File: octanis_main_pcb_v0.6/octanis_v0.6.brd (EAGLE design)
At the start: 80 x 48 mm, 103 parts, among them IC1 BME280, IC2 BNO055A, Q1 32.768kHz, Q2 32.768kHz, U1 TPS61232, U10 INA210, U11 INA210, U12 INA210, U13 RN2483, U2 DRV8836DSSR, U3 DRV8836DSSR, U4 MSP432, U5 SST25VF064C, U6 DRV8836DSSR, U7 DRV8836DSSR, U8 MAX6001SOT-23, U9 INA210

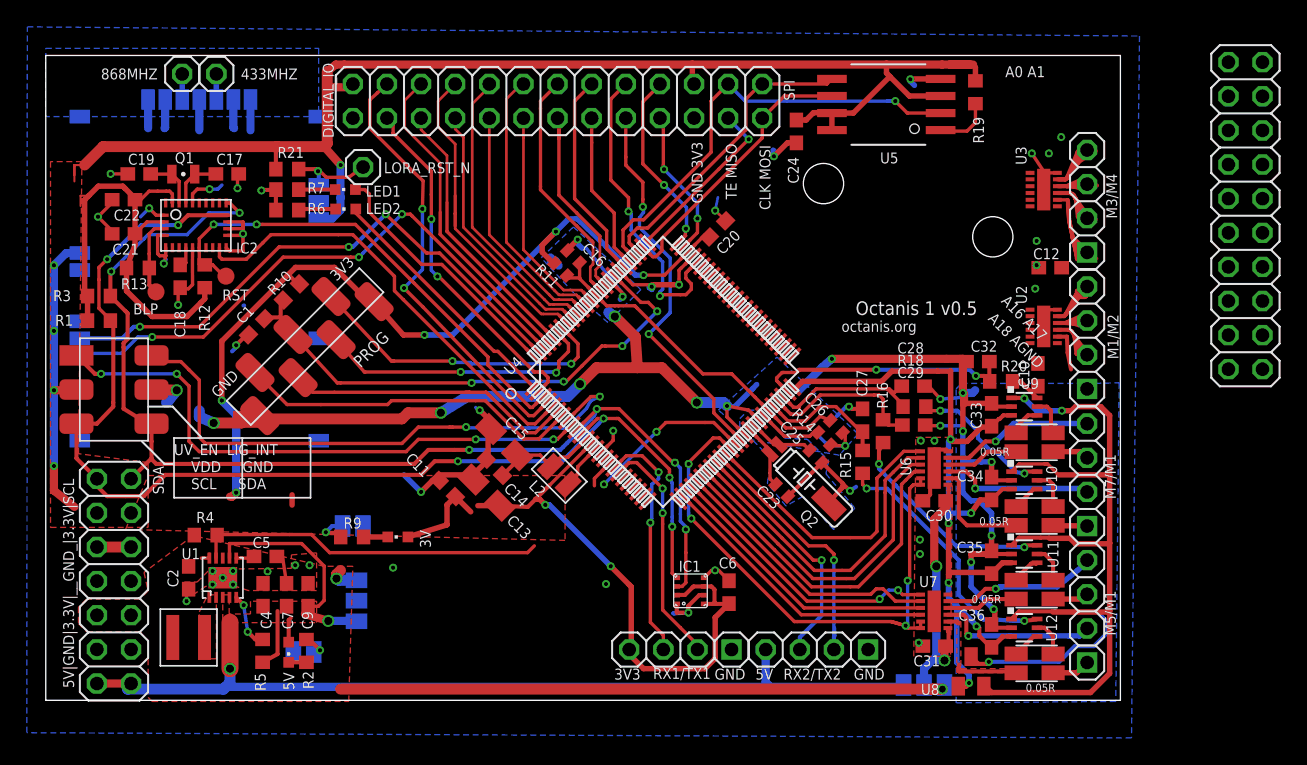
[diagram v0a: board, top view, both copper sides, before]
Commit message: finalized changes for v0.6. coax connector missing
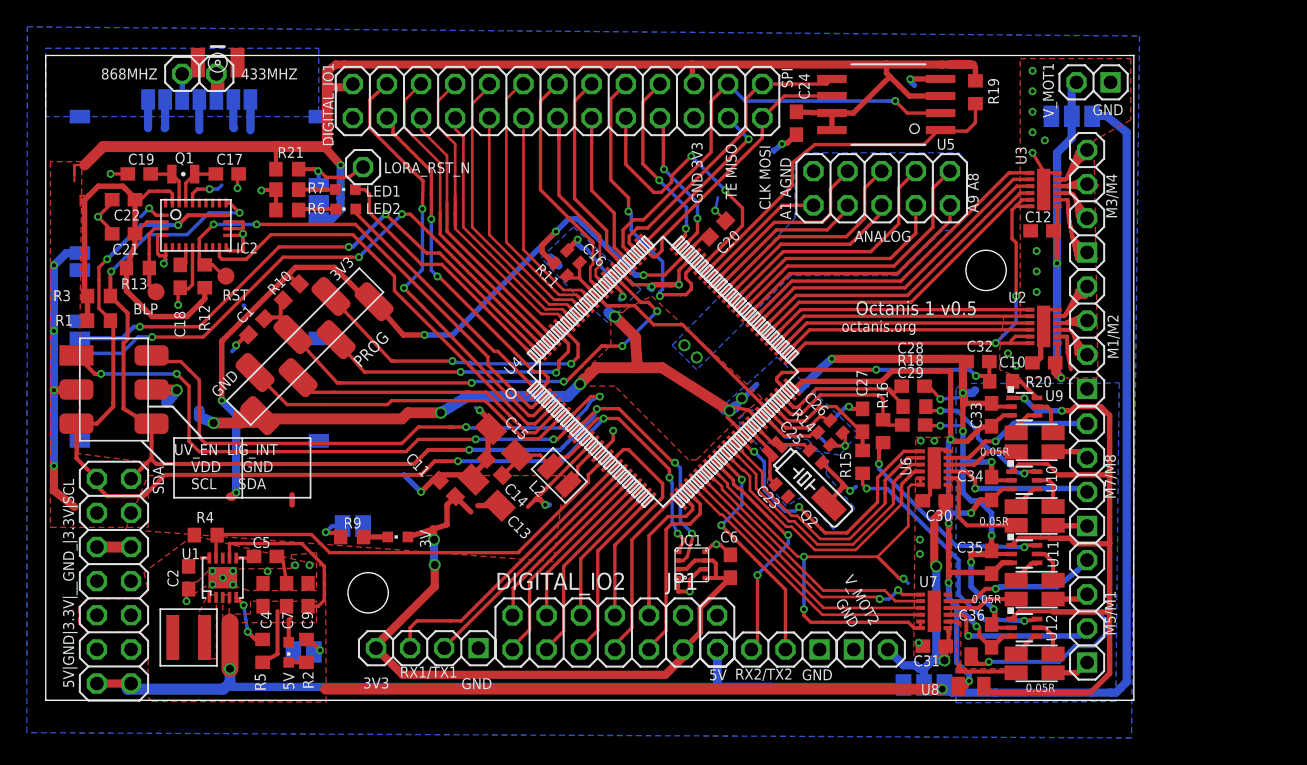
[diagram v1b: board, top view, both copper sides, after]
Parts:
- added DIGITAL_IO2: (no value), pinhead:2X05
- added JP1: (no value), pinhead:2X02
- added V_MOT1, V_MOT2: (no value), pinhead-2:1X02-S
- added X1: MC-921, con-coax:MC-921
- ANALOG: device pinhead:2X10 -> pinhead:2X05
- moved VMOT_SEL 64.3 mm to (76.4, 44.5), turned to 0 degrees
- moved ANALOG 27.2 mm to (62.2, 39.1), turned to 0 degrees
- moved RX1/TX1 18.8 mm to (28.4, 4.88)
- moved RX2/TX2 3.61 mm to (53.8, 4.78)
- moved C12 2.81 mm to (74.2, 35.9)
- moved C6 1.93 mm to (51.0, 11.0)
- moved IC1 1.93 mm to (48.1, 11.1)
- moved C10 0.99 mm to (74.3, 26.1), turned to 0 degrees
- moved C24 0.61 mm to (55.9, 44.0)
- renumbered DIGITAL_IO to DIGITAL_IO1, M7/M1 to M7/M8
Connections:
- removed net A0: ANALOG.1
- removed net P3.7: DIGITAL_IO1.6, U4.39
- removed net P5.6_NC: U4.70
- new net P10.4: DIGITAL_IO2.6, U4.24
- new net P10.5: DIGITAL_IO2.5, U4.25
- new net P2.1: DIGITAL_IO2.8, U4.17
- new net P2.4: DIGITAL_IO2.2, U4.20
- new net P2.5: DIGITAL_IO2.1, U4.21
- new net P2.6: DIGITAL_IO2.4, U4.22
- new net P2.7: DIGITAL_IO2.3, U4.23
- new net P5.6: DIGITAL_IO1.6, U4.70
- new net P7.4: DIGITAL_IO2.7, U4.26
- new net P7.5: DIGITAL_IO2.10, U4.27
- new net P7.6: DIGITAL_IO2.9, U4.28
- net +3V3: now also JP1.1
- net +5V: now also JP1.3; no longer VMOT_SEL.3
- net 5VEN: now also U4.16; no longer U4.17
- net A1: now also ANALOG.1; no longer ANALOG.2
- net A2: now also ANALOG.4; no longer ANALOG.3
- net A3: now also ANALOG.3; no longer ANALOG.4
- net A4: now also ANALOG.6; no longer ANALOG.5
- net A5: now also ANALOG.5; no longer ANALOG.6
- net A6: now also ANALOG.8; no longer ANALOG.7
- net A7: now also ANALOG.7; no longer ANALOG.8
- net A8: now also ANALOG.10; no longer ANALOG.9
- net A9: now also ANALOG.9; no longer ANALOG.10
- net AGND: now also ANALOG.2
- net GND: now also JP1.2, JP1.4, V_MOT1.1, V_MOT2.1, X1.2@1, X1.2@2
- net M1234SLEEP: no longer U4.16
- net M1IN1: no longer U4.38
- net M1IN2: no longer U4.20
- net M2IN1: no longer U4.21
- net M2IN2: no longer U4.22
- net M3IN1: no longer U4.23
- net M3IN2: no longer U4.24
- net M4IN1: no longer U4.25
- net M4IN2: no longer U4.26
- net M5678SLEEP: now also U4.33; no longer U4.37
- net M5IN1: now also U4.29; no longer U4.27
- net M5IN2: now also U4.30; no longer U4.28
- net M6IN1: now also U4.32; no longer U4.30
- net M6IN2: now also U4.31; no longer U4.29
- net M7IN1: now also U4.36; no longer U4.31
- net M7IN2: now also U4.37; no longer U4.32
- net M8IN1: now also U4.38; no longer U4.33
- net M8IN2: now also U4.39; no longer U4.36
- net V_MOTOR: now also V_MOT1.2
- net V_MOTOR2: now also V_MOT2.2
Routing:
- net 3V3_MODULE2: track 49.1 -> 106.0 mm, vias 2 -> 1
- net M1234SLEEP: track 0.00 -> 33.8 mm, vias 0 -> 2
- net V_MOTOR: track 0.00 -> 30.1 mm, vias 0 -> 2
- net P3.7: track 29.4 -> 0.00 mm, vias 2 -> 0
- net M4IN2: track 0.03 -> 25.0 mm
- net M4IN1: track 0.00 -> 24.6 mm
- net M3IN2: track 0.00 -> 24.2 mm
- net M3IN1: track 0.00 -> 23.8 mm
- net SPI_FLASH_CS: track 4.30 -> 26.9 mm
- net P5.6: track 0.00 -> 21.6 mm, vias 0 -> 2
- net A8: track 0.00 -> 21.2 mm
- net M2IN2: track 0.00 -> 20.0 mm
- net M2IN1: track 0.00 -> 19.6 mm
- net M1IN2: track 0.00 -> 19.1 mm
- net A9: track 0.00 -> 18.9 mm
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- added copper zone on layer 1, net AGND
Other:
- board size 80 x 48 mm -> 81 x 48 mm
- board text added: "A1 AGND"
- board text added: "A9 A8"
- board text removed: "A0 A1"
- board text removed: "A16 A17"
- board text removed: "A18 AGND"

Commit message: added SMA connector for LoRa
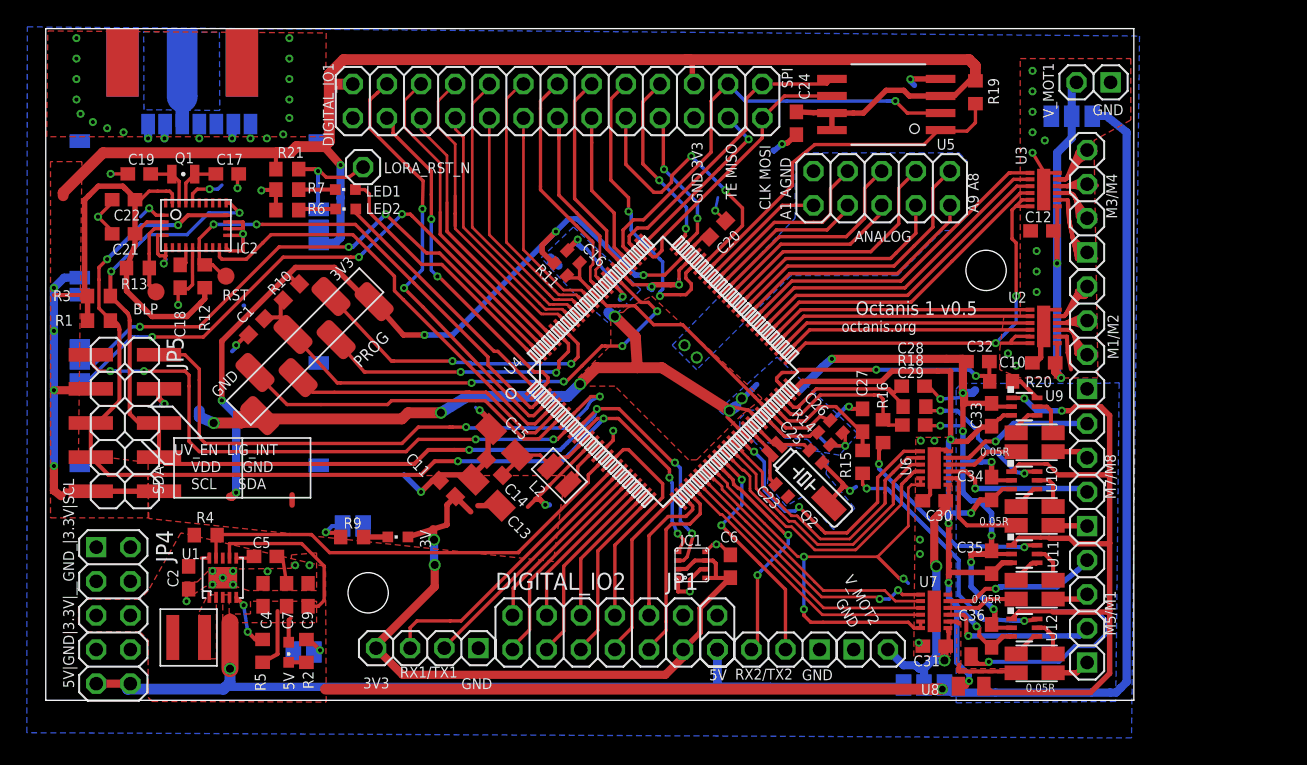
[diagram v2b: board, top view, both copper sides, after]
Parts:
- removed 433MHZ, 868MHZ: (no value), Headerlibrary:1X01
- removed J1: (no value), Seeed-OPL-Connector:H2X3-SMD-2.54
- removed JP2: (no value), pinhead:2X07
- removed X1: MC-921, con-coax:MC-921
- added JP4: (no value), pinhead-2:2X05
- added JP5: (no value), pinhead-2:2X05SMD
- added X3: (no value), sma_end_launch:SMA_EDGELAUNCH
- moved U13 1.83 mm to (20.3, 17.2)
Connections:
- net +3V3: now also JP5.10, JP5.3, JP5.9; no longer J1.2, JP2.3, JP2.4
- net +5V: now also JP4.10, JP4.9; no longer JP2.13, JP2.14
- net 3V3_MODULE2: now also JP4.5, JP4.6; no longer JP2.10, JP2.9
- net ANT433: no longer 433MHZ.1
- net ANT868: now also X3.P; no longer 868MHZ.1
- net EXT_LIGHTNING_INT: now also JP5.2; no longer J1.6
- net EXT_UV_EN: now also JP5.1; no longer J1.1
- net GND: now also JP4.1, JP4.2, JP4.3, JP4.4, JP4.7, JP4.8, JP5.4, X3.GND@1, X3.GND@2, X3.GND@3, X3.GND@4; no longer J1.5, JP2.11, JP2.12, JP2.5, JP2.6, JP2.7, JP2.8, X1.2@1, X1.2@2
- net SCL: now also JP5.5, JP5.7; no longer J1.3, JP2.1
- net SDA: now also JP5.6, JP5.8; no longer J1.4, JP2.2
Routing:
- net GND: track 122.4 -> 111.5 mm, vias 43 -> 63
- net +3V3: track 298.7 -> 305.1 mm
- net ANT868: track 1.91 -> 6.42 mm
- net SCL: track 86.6 -> 84.2 mm
- net ANT433: track 1.91 -> 0.00 mm
- net LORA_RST_N: track 6.32 -> 8.22 mm
- net SDA: track 84.5 -> 82.9 mm
- net RX3: track 42.9 -> 43.7 mm
- net TX3: track 42.2 -> 42.9 mm
- net +5V: track 95.0 -> 94.3 mm
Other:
- board size 81 x 48 mm -> 81 x 50 mm

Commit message: DRC clean layout
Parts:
- moved U$1 1.75 mm to (16.4, 18.1)
- moved V_MOT1 1.30 mm to (76.8, 47.5)
- moved R4 0.54 mm to (11.5, 12.9)
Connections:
- new net V_MOTOR_ALT: VMOT_SEL.3, V_MOT1.2
- net V_MOTOR: no longer V_MOT1.2
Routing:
- net GND: track 111.5 -> 115.2 mm
- net V_MOTOR_ALT: track 0.00 -> 3.25 mm
- net M5678SLEEP: track 40.0 -> 36.9 mm, vias 3 -> 2
- net V_MOTOR: track 30.1 -> 27.4 mm
- net N$49: track 3.18 -> 5.02 mm
- net N$39: track 3.10 -> 4.55 mm
- net M7IN2: track 21.1 -> 22.1 mm
- net 5VEN: track 34.5 -> 35.5 mm
- net M8IN2: track 21.4 -> 22.3 mm
- net M8IN1: track 21.0 -> 21.8 mm
- net M7IN1: track 21.7 -> 22.5 mm
- net 3V3_MODULE2: track 106.0 -> 105.4 mm
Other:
- board text added: "5V|GND|3.3V|__GND_|"
- board text added: "A8 A9"
- board text added: "AGND A1"
- board text added: "Octanis 1 v0.6"
- board text removed: "5V|GND|3.3V|__GND_|3.3V|SCL"
- board text removed: "A1 AGND"
- board text removed: "A9 A8"
- board text removed: "Octanis 1 v0.5"
- board text removed: "SDA"

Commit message: revised silklayer
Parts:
- removed C35, C36: 10n, rcl:C0603
- removed JP4: (no value), pinhead-2:2X05
- removed R20: 6.8k, rcl:R0603
- removed R21: 100k, rcl:R0603
- added C3: 100n, rcl:C0603
- added C8: 22uF, rcl:C0603
- added JP3: (no value), pinhead:2X02
- added R17: 6.8k, rcl:R0603
- added R8: 1k, rcl:R0603
- C1: value 1n -> 22uF
- C10: value 470n -> 10nF
- C11: value 100n -> 1n
- C12: value 470n -> 10u; device rcl:C0603 -> rcl:A/3216-18R
- C13: value 10u -> 100n; device rcl:A/3216-18R -> rcl:C0603
- C17: value 12p -> 100n
- C18: value 100n -> 12p; device rcl:C0603 -> rcl:C0402
- C19, C20: device rcl:C0603 -> rcl:C0402
- C2: value 22uF -> 100n
- C22: value 120n -> 100n
- C23: value 12p -> 470n; device rcl:C0402 -> rcl:C0603
- C24: value 100n -> 10n
- C25: value 12p -> 10n; device rcl:C0402 -> rcl:C0603
- C26: value 100n -> 470n; device rcl:C0402 -> rcl:C0603
- C27, C30: value 470n -> 10n
- C33, C34: value 10n -> 470n
- C4: value 22uF -> 120n
- C5: value 10nF -> 12p
- C6: value 100n -> 12p
- IC1: value BME280 -> BNO055A; device bosch-bme280:BME280 -> BNO055:BNO055
- IC2: value BNO055A -> BME280; device BNO055:BNO055 -> bosch-bme280:BME280
- JP1: device pinhead:2X02 -> pinhead-2:2X05
- LED1: value LED0 -> LED1
- LED2: value LED1 -> LED0
- R1: value 4.7k -> 1M
- R10: value 47k -> 1k
- R11: value 0R -> 1k; device rcl:R0402 -> rcl:R0603
- R13: value 100k -> 0R; device rcl:R0603 -> rcl:R0402
- R18: value 6.8k -> 10k
- R19: value 10k -> 6.8k
- R2: value 1k -> 4.7k
- R4, R5: value 1M -> 100k
- R7: value 1k -> 1M
- R9: value 1k -> 47k
- U11, U12: value INA210 -> DRV8836DSSR; device Octanis1_EPS:SC70-6 -> DRV8834:SON50P200X300X80-13N
- U2: value DRV8836DSSR -> MSP432; device DRV8834:SON50P200X300X80-13N -> MSP-EXP432:PZ100
- U3: value DRV8836DSSR -> MAX6001SOT-23; device DRV8834:SON50P200X300X80-13N -> Octanis1:MAX6001
- U4: value MSP432 -> DRV8836DSSR; device MSP-EXP432:PZ100 -> DRV8834:SON50P200X300X80-13N
- U5: value SST25VF064C -> DRV8836DSSR; device BertaLib:SOIC_8-LEAD -> DRV8834:SON50P200X300X80-13N
- U6: value DRV8836DSSR -> SST25VF064C; device DRV8834:SON50P200X300X80-13N -> BertaLib:SOIC_8-LEAD
- U7: value DRV8836DSSR -> INA210; device DRV8834:SON50P200X300X80-13N -> Octanis1_EPS:SC70-6
- U8: value MAX6001SOT-23 -> INA210; device Octanis1:MAX6001 -> Octanis1_EPS:SC70-6
- moved C10 59.7 mm to (16.4, 11.7)
- moved C19 54.6 mm to (57.3, 19.2), turned to 135 degrees
- moved C22 50.4 mm to (55.9, 44.0), turned to 270 degrees
- moved C18 47.5 mm to (54.8, 16.6), turned to 135 degrees
- moved C17 47.5 mm to (51.0, 11.0), turned to 90 degrees
- moved C6 47.5 mm to (13.5, 40.2), turned to 0 degrees
- moved C12 45.7 mm to (32.8, 16.5), turned to 315 degrees
- moved V_MOT1 45.4 mm to (61.4, 4.78), turned to 0 degrees
- moved V_MOT2 45.4 mm to (76.8, 47.5), turned to 180 degrees
- moved IC1 44.7 mm to (11.2, 36.4), turned to 90 degrees
- moved IC2 44.7 mm to (48.1, 11.1), turned to 270 degrees
- moved C21 44.2 mm to (50.0, 36.1), turned to 225 degrees
- moved JP1 43.7 mm to (5.03, 7.32), turned to 270 degrees
- moved C24 40.8 mm to (70.4, 5.79)
- moved U3 36.3 mm to (68.9, 3.15), turned to 0 degrees
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- renumbered JP5 to JP2, M5/M1 to M5/M6, U$100 to U$2, U13 to U100, VMOT_SEL2 to VMOT_SEL100, X3 to 868MHZ
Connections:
- net +3V3: now also C12.+, C13.2, C17.1, C21.2, C3.1, C4.1, IC1.28, IC1.3, IC2.2, IC2.6, IC2.8, JP3.1, R12.2, R18.2, R2.2, R4.1, R5.2, R9.1, U2.13, U2.73, U6.RST/HOLD, U6.VDD, U6.WP; no longer C11.2, C13.+, C20.2, C21.1, C24.1, C6.1, IC1.2, IC1.6, IC1.8, IC2.28, IC2.3, JP1.1, R1.2, R10.1, R11.2, R12.1, R19.2, R21.2, U4.13, U4.73, U5.RST/HOLD, U5.VDD, U5.WP
- net +5V: now also C8.1, JP1.10, JP1.9, JP3.3, R7.2; no longer C4.1, JP1.3, JP4.10, JP4.9, R5.2
- net 3V3_MODULE2: now also C1.1, JP1.5, JP1.6, R1.2; no longer C2.1, JP4.5, JP4.6, R4.2
- net 5VEN: now also R1.1, U2.16; no longer R4.1, U4.16
- net A1: now also U2.68; no longer U4.68
- net A2: now also U2.67; no longer U4.67
- net A20: now also R19.1, U2.49; no longer R20.1, U4.49
- net A20UNF: now also R19.2, U10.6; no longer R20.2, U9.6
- net A21: now also C31.2, R17.1, U2.48; no longer C28.2, R18.1, U4.48
- net A21UNF: now also R17.2, U9.6; no longer R18.2, U10.6
- net A22: now also C28.2, U2.47; no longer C29.2, U4.47
- net A22UNF: now also U8.6; no longer U11.6
- net A23: now also C29.2, U2.46; no longer C27.2, U4.46
- net A23UNF: now also U7.6; no longer U12.6
- net A3: now also U2.66; no longer U4.66
- net A4: now also U2.65; no longer U4.65
- net A5: now also U2.64; no longer U4.64
- net A6: now also U2.63; no longer U4.63
- net A7: now also U2.62; no longer U4.62
- net A8: now also U2.61; no longer U4.61
- net A9: now also U2.60; no longer U4.60
- net ACCEL_INT: now also IC1.14, U2.5; no longer IC2.14, U4.5
- net ACCEL_N_BOOTLD: now also IC1.4, R5.1; no longer IC2.4, R13.1
- net ACCEL_N_RST: now also IC1.11, R4.2, U2.3; no longer IC2.11, R12.2, U4.3
- net AGND: now also C20.2, C24.1, C25.1, C30.1, C31.1, U2.40, U2.43, U2.84, U3.3, U7.2, U8.2; no longer C26.2, C33.1, C34.1, C35.1, C36.1, U11.2, U12.2, U4.40, U4.43, U4.84, U8.3
- net AVCC: now also C20.1, R13.1, U2.45, U2.87; no longer C26.1, R11.1, U4.45, U4.87
- net CURR_SENSE_EN: now also C24.2, C25.2, C27.2, C30.2, U2.50, U3.1, U7.3, U8.3; no longer C33.2, C34.2, C35.2, C36.2, U11.3, U12.3, U4.50, U8.1
- net EXT_LIGHTNING_INT: now also U2.8; no longer U4.8
- net EXT_UV_EN: now also U2.9; no longer U4.9
- net GND: now also C1.2, C10.2, C12.-, C13.1, C19.1, C2.1, C21.1, C26.1, C3.2, C33.1, C34.1, C8.2, IC1.10, IC1.15, IC1.16, IC1.17, IC1.18, IC1.2, IC1.25, IC1.6, IC2.1, IC2.7, JP1.1, JP1.3, JP1.7, JP1.8, JP3.2, JP3.4, R10.1, R11.1, U11.13, U11.6, U12.13, U12.6, U2.15, U2.72, U2.82, U4.13, U4.6, U5.13, U5.6, U6.VSS; no longer C1.1, C10.1, C12.1, C13.-, C19.2, C2.2, C20.1, C21.2, C24.2, C25.1, C30.1, C31.1, IC1.1, IC1.7, IC2.10, IC2.15, IC2.16, IC2.17, IC2.18, IC2.2, IC2.25, IC2.6, JP4.1, JP4.2, JP4.3, JP4.4, JP4.7, JP4.8, R6.1, R7.1, U2.13, U2.6, U3.13, U3.6, U4.15, U4.72, U4.82, U5.VSS, U6.13, U6.6, U7.13, U7.6
- net LED0: now also LED2.A, U2.100; no longer LED1.A, U4.100
- net LED1: now also LED1.A, U2.1; no longer LED2.A, U4.1
- net LORA_RST_N: now also R12.1; no longer R21.1
- net M1234SLEEP: now also U11.11, U11.12, U12.11, U12.12, U2.51; no longer U2.11, U2.12, U3.11, U3.12, U4.51
- net M1IN1: now also U11.10, U2.52; no longer U2.10, U4.52
- net M1IN2: now also U11.9, U2.53; no longer U2.9, U4.53
- net M2IN1: now also U11.8, U2.54; no longer U2.8, U4.54
- net M2IN2: now also U11.7, U2.55; no longer U2.7, U4.55
- net M3IN1: now also U12.10, U2.56; no longer U3.10, U4.56
- net M3IN2: now also U12.9, U2.57; no longer U3.9, U4.57
- net M4IN1: now also U12.8, U2.58; no longer U3.8, U4.58
- net M4IN2: now also U12.7, U2.59; no longer U3.7, U4.59
- net M5678SLEEP: now also U2.33, U4.11, U4.12, U5.11, U5.12; no longer U4.33, U6.11, U6.12, U7.11, U7.12
- net M5IN1: now also U2.29, U4.10; no longer U4.29, U7.10
- net M5IN2: now also U2.30, U4.9; no longer U4.30, U7.9
- net M5OUT1: now also RS1.I1, U4.2; no longer RS4.I1, U7.2
- net M6IN1: now also U2.32, U4.8; no longer U4.32, U7.8
- net M6IN2: now also U2.31, U4.7; no longer U4.31, U7.7
- net M7IN1: now also U2.36, U5.10; no longer U4.36, U6.10
- net M7IN2: now also U2.37, U5.9; no longer U4.37, U6.9
- net M8IN1: now also U2.38, U5.8; no longer U4.38, U6.8
- net M8IN2: now also U2.39, U5.7; no longer U4.39, U6.7
- net N$1: now also U2.12; no longer U4.12
- net N$10: now also C19.2, U2.42; no longer C25.2, U4.42
- net N$13: now also U12.2; no longer U3.2
- net N$14: now also R6.1; no longer R2.1
- net N$15: now also RS1.V2, U7.5; no longer RS4.V2, U12.5
- net N$17: now also RS1.V1, U7.4; no longer RS4.V1, U12.4
- net N$18: now also C2.2, IC1.9; no longer C18.2, IC2.9
- net N$19: now also C5.1, IC1.27; no longer C19.1, IC2.27
- net N$2: now also R7.1; no longer R5.1
- net N$21: now also RS1.I2; no longer RS4.I2
- net N$23: now also RS2.V1, U8.4; no longer RS3.V1, U11.4
- net N$24: now also RS2.V2, U8.5; no longer RS3.V2, U11.5
- net N$25: now also RS2.I1, U4.4; no longer RS3.I1, U7.4
- net N$26: now also R8.1; no longer R9.1
- net N$27: now also RS2.I2; no longer RS3.I2
- net N$28: now also RS3.V2, U9.5; no longer RS2.V2, U10.5
- net N$29: now also RS3.V1, U9.4; no longer RS2.V1, U10.4
- net N$30: now also RS4.V2, U10.5; no longer RS1.V2, U9.5
- net N$31: now also RS4.V1, U10.4; no longer RS1.V1, U9.4
- net N$32: now also RS3.I2; no longer RS2.I2
- net N$33: now also U2.44; no longer U4.44
- net N$34: now also U2.14; no longer U4.14
- net N$35: now also RS4.I1, U5.4; no longer RS1.I1, U6.4
- net N$36: now also RS3.I1, U5.2; no longer RS2.I1, U6.2
- net N$37: now also RS4.I2; no longer RS1.I2
- net N$38: now also U4.3; no longer U7.3
- net N$39: now also U12.3; no longer U3.3
- net N$4: now also R8.2; no longer R9.2
- net N$40: now also U12.4; no longer U3.4
- net N$41: now also U12.5; no longer U3.5
- net N$42: now also C10.1; no longer C5.1
- net N$43: now also U4.5; no longer U7.5
- net N$44: now also R6.2; no longer R2.2
- net N$45: now also U5.5; no longer U6.5
- net N$49: now also U11.2; no longer U2.2
- net N$5: now also LED2.C, R11.2; no longer LED1.C, R7.2
- net N$50: now also U11.3; no longer U2.3
- net N$51: now also U11.4; no longer U2.4
- net N$52: now also U11.5; no longer U2.5
- net N$54: now also U5.3; no longer U6.3
- net N$6: now also LED1.C, R10.2; no longer LED2.C, R6.2
- net N$73: now also C6.1, IC1.26; no longer C17.1, IC2.26
- net N$76: now also U2.94; no longer U4.94
- net N$77: now also U2.95; no longer U4.95
- net N$8: now also C18.2, U2.41; no longer C23.2, U4.41
- net P1.0: now also U2.4; no longer U4.4
- net P10.2: now also U2.2; no longer U4.2
- net P10.4: now also U2.24; no longer U4.24
- net P10.5: now also U2.25; no longer U4.25
- net P2.1: now also U2.17; no longer U4.17
- net P2.4: now also U2.20; no longer U4.20
- net P2.5: now also U2.21; no longer U4.21
- net P2.6: now also U2.22; no longer U4.22
- net P2.7: now also U2.23; no longer U4.23
- net P5.6: now also U2.70; no longer U4.70
- net P5.7: now also U2.71; no longer U4.71
- net P6.6: now also U2.80; no longer U4.80
- net P6.7: now also U2.81; no longer U4.81
- net P7.0: now also U2.88; no longer U4.88
- net P7.1: now also U2.89; no longer U4.89
- net P7.2: now also U2.90; no longer U4.90
- net P7.3: now also U2.91; no longer U4.91
- net P7.4: now also U2.26; no longer U4.26
- net P7.5: now also U2.27; no longer U4.27
- net P7.6: now also U2.28; no longer U4.28
- net P9.2: now also U2.74; no longer U4.74
- net P9.3: now also U2.75; no longer U4.75
- net P9.4: now also U2.96; no longer U4.96
- net P9.5: now also U2.97; no longer U4.97
- net PJ.2: now also U2.85; no longer U4.85
- net PJ.3: now also U2.86; no longer U4.86
- net PJ.4: now also U2.92; no longer U4.92
- net PJ.5: now also U2.93; no longer U4.93
- net RST_N: now also C11.2, R9.2, U2.83; no longer C1.2, R10.2, U4.83
- net RX0: now also U2.6; no longer U4.6
- net RX1: now also U2.18; no longer U4.18
- net RX2: now also U2.34; no longer U4.34
- net RX3: now also U2.98; no longer U4.98
- net SCL: now also IC1.19, IC2.4, R2.1, U2.11; no longer IC1.4, IC2.19, R1.1, U4.11
- net SDA: now also IC1.20, IC2.3, U2.10; no longer IC1.3, IC2.20, U4.10
- net SPI_EXTSLAVE_TE: now also U2.76; no longer U4.76
- net SPI_FLASH_CS: now also R18.1, U2.69, U6.CE; no longer R19.1, U4.69, U5.CE
- net SPI_MISO: now also U2.79, U6.SO; no longer U4.79, U5.SO
- net SPI_MOSI: now also U2.78, U6.SI; no longer U4.78, U5.SI
- net SPI_SCK: now also U2.77, U6.SCK; no longer U4.77, U5.SCK
- net TX0: now also U2.7; no longer U4.7
- net TX1: now also U2.19; no longer U4.19
- net TX2: now also U2.35; no longer U4.35
- net TX3: now also U2.99; no longer U4.99
- net VREF_M: now also U3.2, U7.1, U8.1; no longer U11.1, U12.1, U8.2
- net V_MOTOR: now also C33.2, C34.2, U11.1, U12.1; no longer C10.2, C12.2, U2.1, U3.1
- net V_MOTOR2: now also C23.2, C26.2, U4.1, U5.1, V_MOT1.2; no longer C30.2, C31.2, U6.1, U7.1, V_MOT2.2
- net V_MOTOR_ALT: now also V_MOT2.2; no longer V_MOT1.2
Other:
- board text added: "3V3 V_mot V_ext"
- board text added: "5V|GND|_3V3|__GND_|"
- board text removed: "5V V_mot 3V3"
- board text removed: "5V|GND|3.3V|__GND_|"

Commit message: created gerber
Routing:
- net GND: vias 63 -> 62
